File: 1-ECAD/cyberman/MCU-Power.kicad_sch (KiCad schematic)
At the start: 12 parts, among them U1 ESP32-S3R16V

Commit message: update power sche
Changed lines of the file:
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@@
+		)
+	)
+	(text_box "DESIGN NOTE:\nVoltage of VDD_SPI is 1.8V"
+		(exclude_from_sim no)
+		(at 63.5 92.71 0)
+		(size 30.48 20.32)
+		(stroke
+			(width 1)
+			(type solid)
+			(color 200 200 200 1)
+		)
+		(fill
+			(type none)
+		)
+		(effects
+			(font
+				(face "Times New Roman")
+				(size 2 2)
+				(color 0 0 0 1)
+			)
+			(justify left top)
 		)
 	)

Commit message: microSD and LCD connector
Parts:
- U1: Manufacturer (none) -> Espressif; Manufacturer PN (none) -> ESP32-S3R16V; Supplier 1 (none) -> Mouser; Supplier PN 1 (none) -> 356-ESP32-S3R16V; kode PN (none) -> DOTU001
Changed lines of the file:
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@@
 			)
 		)
-		(property "Description" "Xtensa 32-bit dual-core, Wi-Fi/Bluetooth, 16MB PSRAM, 45 GPIOS, QFN56"
+		(property "Description" "Espressif Xtensa 32-bit dual-core, Wi-Fi/Bluetooth, 16MB PSRAM, 45 GPIOS, QFN56"
 			(at 203.2 50.8 0)
 			(effects
@@
 		)
 		(property "kode_PN" "DOTU001"
+			(at 203.2 50.8 0)
+			(effects
+				(font
+					(size 1.27 1.27)
+				)
+				(hide yes)
+			)
+		)
+		(property "kode PN" "DOTU001"
+			(at 203.2 50.8 0)
+			(effects
+				(font
+					(size 1.27 1.27)
+				)
+				(hide yes)
+			)
+		)
+		(property "Manufacturer" "Espressif"
+			(at 203.2 50.8 0)
+			(effects
+				(font
+					(size 1.27 1.27)
+				)
+				(hide yes)
+			)
+		)
+		(property "Manufacturer PN" "ESP32-S3R16V"
+			(at 203.2 50.8 0)
+			(effects
+				(font
+					(size 1.27 1.27)
+				)
+				(hide yes)
+			)
+		)
+		(property "Supplier 1" "Mouser"
+			(at 203.2 50.8 0)
+			(effects
+				(font
+					(size 1.27 1.27)
+				)
+				(hide yes)
+			)
+		)
+		(property "Supplier PN 1" "356-ESP32-S3R16V"
 			(at 203.2 50.8 0)
 			(effects
@@
 			)
 		)
-		(property "Description" "Power symbol creates a global label with name \"VDD_SPI\""
+		(property "Description" "Power symbol creates a global label with name \"VDD\""
 			(at 180.34 73.66 0)
 			(effects

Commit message: esp and usbc footprints
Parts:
- U1: footprint (none) -> 0_mcu_espressif:ESP32-S3R16V
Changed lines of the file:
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@@
 			)
 		)
-		(property "Footprint" ""
+		(property "Footprint" "0_mcu_espressif:ESP32-S3R16V"
 			(at 209.55 38.1 0)
 			(effects

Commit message: footpritn day
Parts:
- U1: Supplier 1 PN (none) -> 356-ESP32-S3R16V; Supplier PN 1 356-ESP32-S3R16V -> (none); kode_PN DOTU001 -> (none)
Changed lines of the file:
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@@
+	)
+	(symbol
+		(lib_id "Device:L")
+		(at 158.75 96.52 90)
+		(unit 1)
+		(exclude_from_sim no)
+		(in_bom yes)
+		(on_board yes)
+		(dnp no)
+		(property "Reference" "L1"
+			(at 154.94 95.25 90)
+			(effects
+				(font
+					(size 1.27 1.27)
+				)
+			)
+		)
+		(property "Value" "2.0nH(0.1nH)"
+			(at 166.37 95.25 90)
+			(effects
+				(font
+					(size 1.27 1.27)
+				)
+			)
+		)
+		(property "Footprint" ""
+			(at 158.75 96.52 0)
+			(effects
+				(font
+					(size 1.27 1.27)
+				)
+				(hide yes)
+			)
+		)
+		(property "Datasheet" "~"
+			(at 158.75 96.52 0)
+			(effects
+				(font
+					(size 1.27 1.27)
+				)
+				(hide yes)
+			)
+		)
+		(property "Description" "Inductor"
+			(at 158.75 96.52 0)
+			(effects
+				(font
+					(size 1.27 1.27)
+				)
+				(hide yes)
+			)
+		)
+		(pin "1"
+		)
+		(pin "2"
+		)
+		(instances
+			(project "cyberman"
+				(path "/0650c7a8-acba-429c-9f8e-eec0baf0bc1c/fede4c36-00cc-4d3d-b71c-5243ba232202/e46a9372-83c8-4117-b39c-2866170a3986"
+					(reference "L1")
+					(unit 1)
+				)
+			)
+		)
 	)
 	(symbol
@@
 			)
 		)
-		(property "kode_PN" "DOTU001"
-			(at 203.2 50.8 0)
-			(effects
-				(font
-					(size 1.27 1.27)
-				)
-				(hide yes)
-			)
-		)
 		(property "kode PN" "DOTU001"
 			(at 203.2 50.8 0)
@@
 			)
 		)
-		(property "Supplier PN 1" "356-ESP32-S3R16V"
+		(property "Supplier 1 PN" "356-ESP32-S3R16V"
 			(at 203.2 50.8 0)
 			(effects
@@
 			)
 		)
+		(pin "2"
+		)
+		(pin "32"
+		)
+		(pin "21"
+		)
+		(pin "47"
+		)
+		(pin "30"
+		)
+		(pin "33"
+		)
+		(pin "34"
+		)
+		(pin "35"
+		)
+		(pin "12"
+		)
+		(pin "25"
+		)
+		(pin "1"
+		)
+		(pin "20"
+		)
+		(pin "53"
+		)
+		(pin "16"
+		)
+		(pin "29"
+		)
+		(pin "3"
+		)
+		(pin "46"
+		)
+		(pin "56"
+		)
+		(pin "57"
+		)
+		(pin "11"
+		)
+		(pin "13"
+		)
+		(pin "14"
+		)
+		(pin "15"
+		)
+		(pin "10"
+		)
+		(pin "17"
+		)
+		(pin "18"
+		)
+		(pin "22"
+		)
+		(pin "24"
+		)
+		(pin "26"
+		)
+		(pin "27"
+		)
+		(pin "23"
+		)
+		(pin "19"
+		)
+		(pin "31"
+		)
+		(pin "6"
+		)
+		(pin "52"
+		)
+		(pin "40"
+		)
+		(pin "43"
+		)
+		(pin "53"
+		)
+		(pin "7"
+		)
+		(pin "49"
+		)
+		(pin "5"
+		)
+		(pin "50"
+		)
+		(pin "44"
+		)
+		(pin "48"
+		)
+		(pin "36"
+		)
+		(pin "51"
+		)
+		(pin "45"
+		)
+		(pin "37"
+		)
+		(pin "42"
+		)
+		(pin "39"
+		)
+		(pin "4"
+		)
+		(pin "38"
+		)
+		(pin "9"
+		)
+		(pin "41"
+		)
+		(pin "8"
+		)
 		(pin "54"
 		)
-		(pin "27"
-		)
-		(pin "10"
-		)
-		(pin "26"
-		)
-		(pin "4"
-		)
-		(pin "53"
-		)
-		(pin "8"
-		)
-		(pin "9"
-		)
-		(pin "47"
-		)
-		(pin "50"
-		)
-		(pin "40"
-		)
-		(pin "44"
-		)
-		(pin "21"
-		)
-		(pin "39"
-		)
-		(pin "41"
-		)
-		(pin "25"
-		)
-		(pin "20"
-		)
-		(pin "31"
-		)
-		(pin "18"
-		)
-		(pin "53"
-		)
-		(pin "33"
-		)
-		(pin "46"
-		)
-		(pin "56"
-		)
-		(pin "19"
-		)
-		(pin "14"
-		)
-		(pin "1"
-		)
-		(pin "13"
-		)
-		(pin "17"
-		)
-		(pin "15"
-		)
-		(pin "48"
-		)
-		(pin "34"
-		)
-		(pin "37"
-		)
-		(pin "42"
-		)
-		(pin "32"
-		)
-		(pin "12"
-		)
-		(pin "57"
-		)
-		(pin "16"
-		)
-		(pin "2"
-		)
-		(pin "36"
-		)
-		(pin "23"
-		)
-		(pin "29"
-		)
-		(pin "22"
-		)
-		(pin "35"
-		)
-		(pin "3"
-		)
-		(pin "38"
-		)
-		(pin "43"
-		)
-		(pin "49"
-		)
-		(pin "5"
-		)
-		(pin "51"
-		)
-		(pin "52"
-		)
-		(pin "45"
-		)
-		(pin "6"
-		)
-		(pin "30"
-		)
-		(pin "24"
-		)
-		(pin "7"
-		)
-		(pin "11"
-		)
-		(instances
-			(project "cyberman"
+		(instances
+			(project ""
 				(path "/0650c7a8-acba-429c-9f8e-eec0baf0bc1c/fede4c36-00cc-4d3d-b71c-5243ba232202/e46a9372-83c8-4117-b39c-2866170a3986"
 					(reference "U1")
-					(unit 1)
-				)
-			)
-		)
-	)
-	(symbol
-		(lib_id "Device:L")
-		(at 158.75 96.52 90)
-		(unit 1)
-		(exclude_from_sim no)
-		(in_bom yes)
-		(on_board yes)
-		(dnp no)
-		(property "Reference" "L1"
-			(at 154.94 95.25 90)
-			(effects
-				(font
-					(size 1.27 1.27)
-				)
-			)
-		)
-		(property "Value" "2.0nH(0.1nH)"
-			(at 166.37 95.25 90)
-			(effects
-				(font
-					(size 1.27 1.27)
-				)
-			)
-		)
-		(property "Footprint" ""
-			(at 158.75 96.52 0)
-			(effects
-				(font
-					(size 1.27 1.27)
-				)
-				(hide yes)
-			)
-		)
-		(property "Datasheet" "~"
-			(at 158.75 96.52 0)
-			(effects
-				(font
-					(size 1.27 1.27)
-				)
-				(hide yes)
-			)
-		)
-		(property "Description" "Inductor"
-			(at 158.75 96.52 0)
-			(effects
-				(font
-					(size 1.27 1.27)
-				)
-				(hide yes)
-			)
-		)
-		(pin "1"
-		)
-		(pin "2"
-		)
-		(instances
-			(project "cyberman"
-				(path "/0650c7a8-acba-429c-9f8e-eec0baf0bc1c/fede4c36-00cc-4d3d-b71c-5243ba232202/e46a9372-83c8-4117-b39c-2866170a3986"
-					(reference "L1")
 					(unit 1)
 				)
@@
 		(dnp no)
 		(fields_autoplaced yes)
-		(property "Reference" "#PWR1"
+		(property "Reference" "#PWR01"
 			(at 215.9 149.86 0)
 			(effects
@@
 			(project "cyberman"
 				(path "/0650c7a8-acba-429c-9f8e-eec0baf0bc1c/fede4c36-00cc-4d3d-b71c-5243ba232202/e46a9372-83c8-4117-b39c-2866170a3986"
-					(reference "#PWR1")
-					(unit 1)
-				)
+					(reference "#PWR01")
+					(unit 1)
+				)

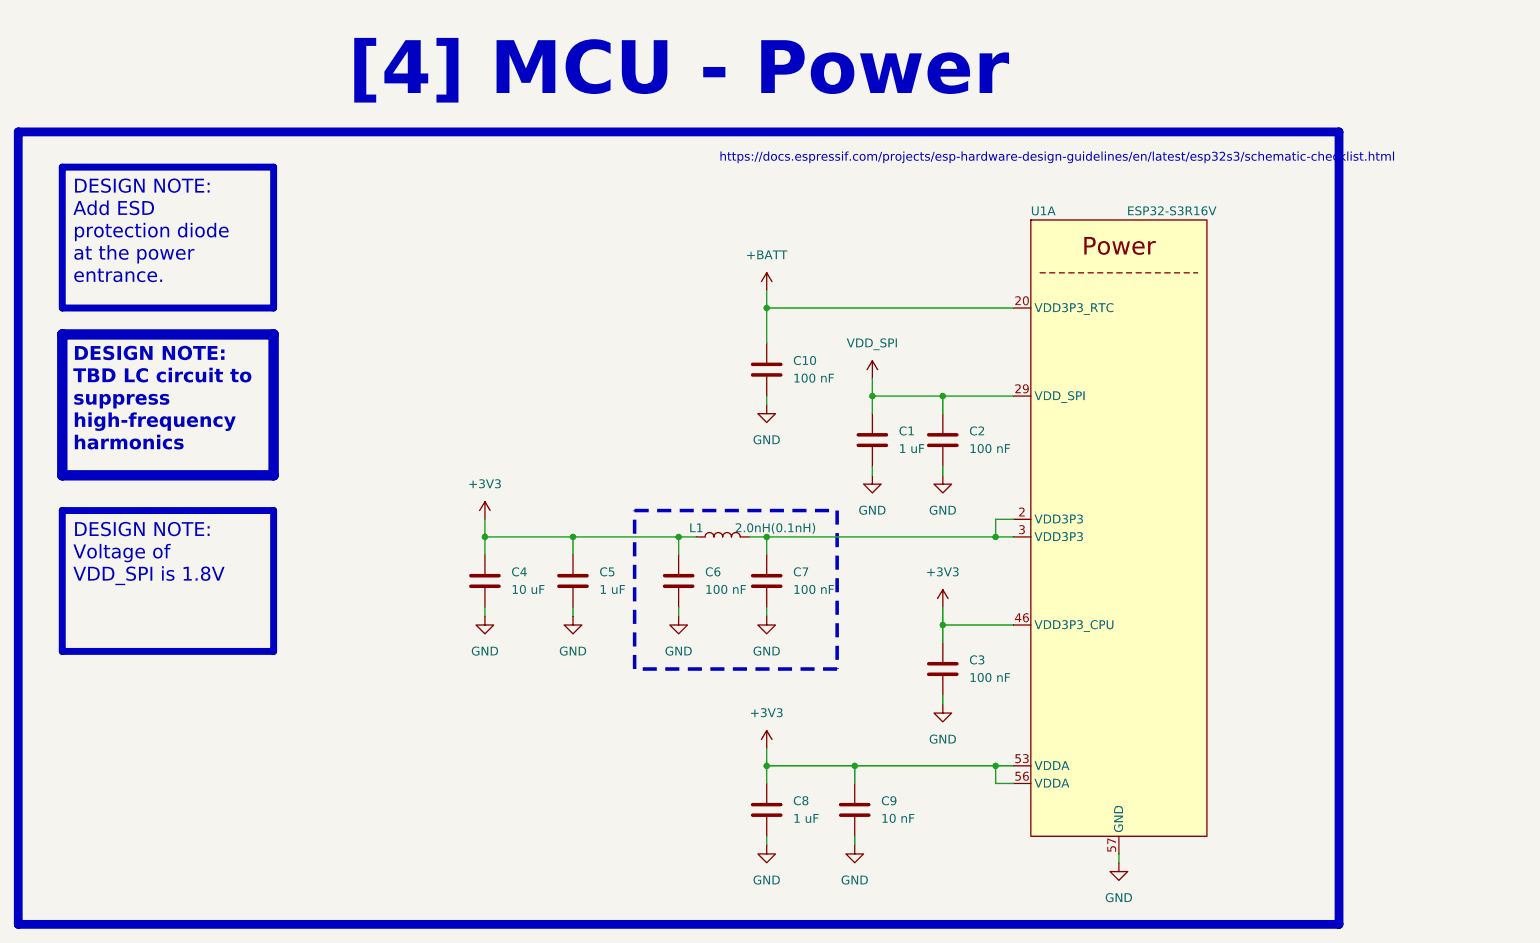
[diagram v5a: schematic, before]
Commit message: new changes
close display page and peripheral schematic
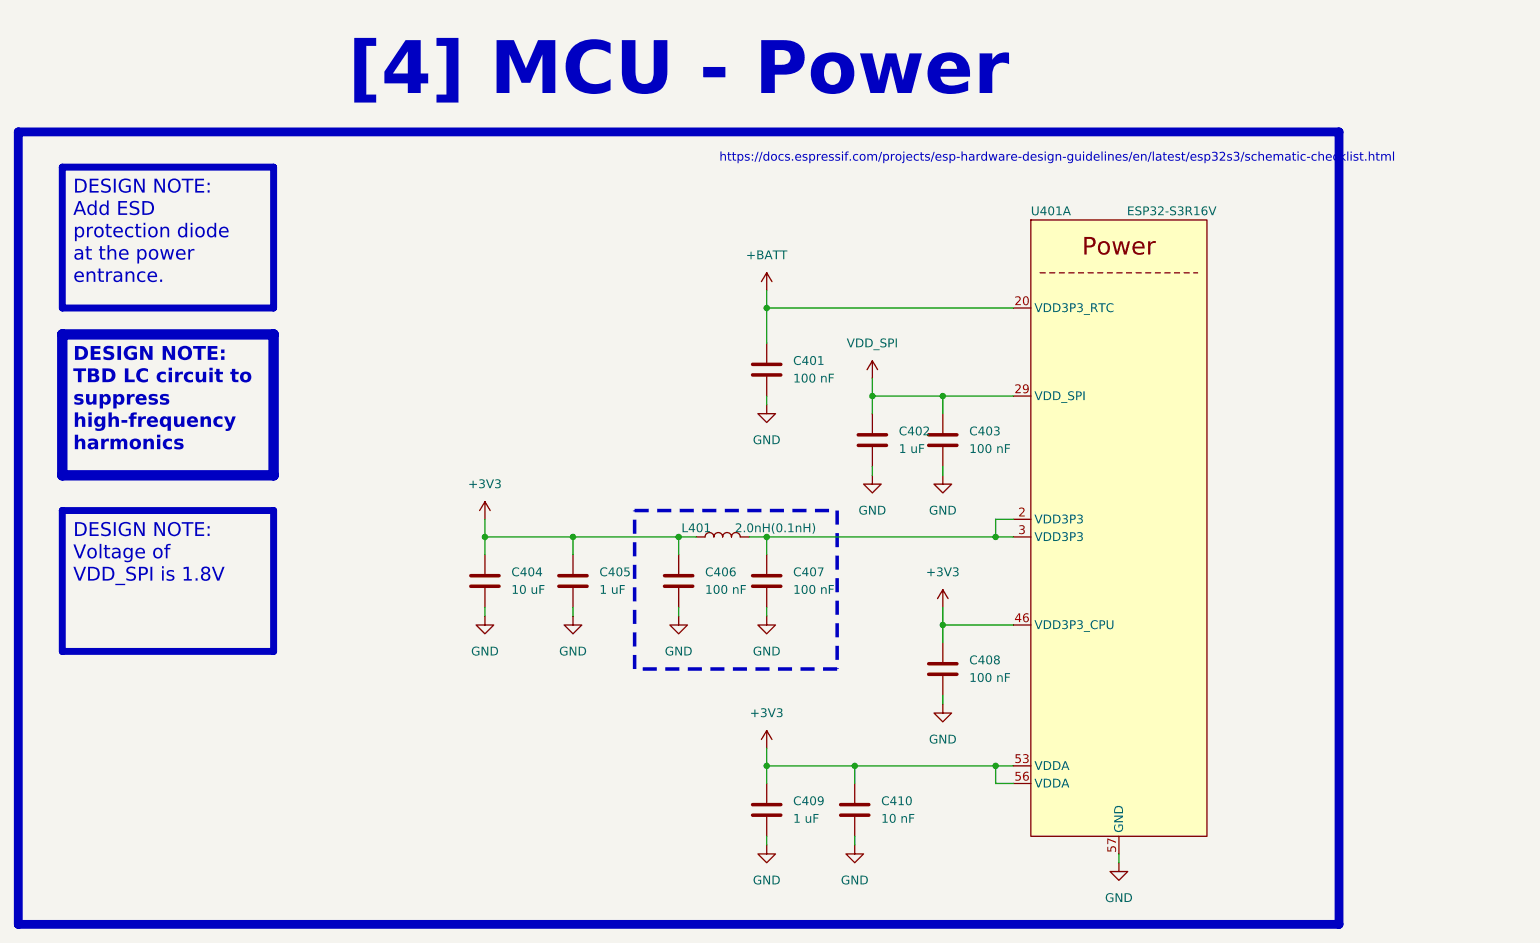
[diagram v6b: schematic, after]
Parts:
- renumbered C10 to C401, C1 to C402, C2 to C403, C4 to C404, C5 to C405, C6 to C406, C7 to C407, C3 to C408, C8 to C409, C9 to C410, L1 to L401, U1 to U401
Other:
- company: (none) -> kode.

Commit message: power page close
siuuuuuuuuuuuu
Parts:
- C401, C403, C406, C407, C408: value 100 nF -> C
- C402, C405, C409: value 1 uF -> C
- C404: value 10 uF -> C
- C410: value 10 nF -> C
- L401: value 2.0nH(0.1nH) -> L
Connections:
- net +BATT renamed +BAT
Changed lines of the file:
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@@
 	(paper "A4")
 	(title_block
-		(date "2024-12-11")
+		(date "2024-12-18")
 		(rev "1.0")
 		(company "kode.")
@@
 			)
 		)
-		(property "Value" "100 nF"
+		(property "Value" "C"
 			(at 168.91 104.14 0)
 			(effects
@@
 		(dnp no)
 		(fields_autoplaced yes)
-		(property "Reference" "#PWR0408"
+		(property "Reference" "#PWR408"
 			(at 124.46 114.3 0)
 			(effects
@@
 			(project "cyberman"
 				(path "/0650c7a8-acba-429c-9f8e-eec0baf0bc1c/fede4c36-00cc-4d3d-b71c-5243ba232202/e46a9372-83c8-4117-b39c-2866170a3986"
-					(reference "#PWR0408")
+					(reference "#PWR408")
 					(unit 1)
 				)
@@
 			)
 		)
-		(property "Value" "100 nF"
+		(property "Value" "C"
 			(at 168.91 73.66 0)
 			(effects
@@
 		(dnp no)
 		(fields_autoplaced yes)
-		(property "Reference" "#PWR0407"
+		(property "Reference" "#PWR407"
 			(at 190.5 110.49 0)
 			(effects
@@
 			(project "cyberman"
 				(path "/0650c7a8-acba-429c-9f8e-eec0baf0bc1c/fede4c36-00cc-4d3d-b71c-5243ba232202/e46a9372-83c8-4117-b39c-2866170a3986"
-					(reference "#PWR0407")
+					(reference "#PWR407")
 					(unit 1)
 				)
@@
 			)
 		)
-		(property "Value" "100 nF"
+		(property "Value" "C"
 			(at 194.31 116.84 0)
 			(effects
@@
 			)
 		)
-		(property "Value" "1 uF"
+		(property "Value" "C"
 			(at 184.15 83.82 0)
 			(effects
@@
 		(dnp no)
 		(fields_autoplaced yes)
-		(property "Reference" "#PWR0401"
+		(property "Reference" "#PWR401"
 			(at 165.1 64.77 0)
 			(effects
@@
 			)
 		)
-		(property "Value" "+BATT"
+		(property "Value" "+BAT"
 			(at 165.1 55.88 0)
 			(effects
@@
 			(project "cyberman"
 				(path "/0650c7a8-acba-429c-9f8e-eec0baf0bc1c/fede4c36-00cc-4d3d-b71c-5243ba232202/e46a9372-83c8-4117-b39c-2866170a3986"
-					(reference "#PWR0401")
+					(reference "#PWR401")
 					(unit 1)
 				)
@@
 			)
 		)
-		(property "Value" "10 uF"
+		(property "Value" "C"
 			(at 128.27 104.14 0)
 			(effects
@@
 		(dnp no)
 		(fields_autoplaced yes)
-		(property "Reference" "#PWR0409"
+		(property "Reference" "#PWR409"
 			(at 137.16 114.3 0)
 			(effects
@@
 			(project "cyberman"
 				(path "/0650c7a8-acba-429c-9f8e-eec0baf0bc1c/fede4c36-00cc-4d3d-b71c-5243ba232202/e46a9372-83c8-4117-b39c-2866170a3986"
-					(reference "#PWR0409")
+					(reference "#PWR409")
 					(unit 1)
 				)
@@
 			)
 		)
-		(property "Value" "1 uF"
+		(property "Value" "C"
 			(at 168.91 137.16 0)
 			(effects
@@
 		(dnp no)
 		(fields_autoplaced yes)
-		(property "Reference" "#PWR0413"
+		(property "Reference" "#PWR413"
 			(at 165.1 130.81 0)
 			(effects
@@
 			(project "cyberman"
 				(path "/0650c7a8-acba-429c-9f8e-eec0baf0bc1c/fede4c36-00cc-4d3d-b71c-5243ba232202/e46a9372-83c8-4117-b39c-2866170a3986"
-					(reference "#PWR0413")
+					(reference "#PWR413")
 					(unit 1)
 				)
@@
 		(dnp no)
 		(fields_autoplaced yes)
-		(property "Reference" "#PWR0411"
+		(property "Reference" "#PWR411"
 			(at 165.1 114.3 0)
 			(effects
@@
 			(project "cyberman"
 				(path "/0650c7a8-acba-429c-9f8e-eec0baf0bc1c/fede4c36-00cc-4d3d-b71c-5243ba232202/e46a9372-83c8-4117-b39c-2866170a3986"
-					(reference "#PWR0411")
+					(reference "#PWR411")
 					(unit 1)
 				)
@@
 		(dnp no)
 		(fields_autoplaced yes)
-		(property "Reference" "#PWR0403"
+		(property "Reference" "#PWR403"
 			(at 165.1 83.82 0)
 			(effects
@@
 			(project "cyberman"
 				(path "/0650c7a8-acba-429c-9f8e-eec0baf0bc1c/fede4c36-00cc-4d3d-b71c-5243ba232202/e46a9372-83c8-4117-b39c-2866170a3986"
-					(reference "#PWR0403")
+					(reference "#PWR403")
 					(unit 1)
 				)
@@
 			)
 		)
-		(property "Value" "100 nF"
+		(property "Value" "C"
 			(at 194.31 83.82 0)
 			(effects
@@
 			)
 		)
-		(property "Value" "2.0nH(0.1nH)"
+		(property "Value" "L"
 			(at 166.37 95.25 90)
 			(effects
@@
 		(dnp no)
 		(fields_autoplaced yes)
-		(property "Reference" "#PWR0404"
+		(property "Reference" "#PWR404"
 			(at 180.34 93.98 0)
 			(effects
@@
 			(project "cyberman"
 				(path "/0650c7a8-acba-429c-9f8e-eec0baf0bc1c/fede4c36-00cc-4d3d-b71c-5243ba232202/e46a9372-83c8-4117-b39c-2866170a3986"
-					(reference "#PWR0404")
+					(reference "#PWR404")
 					(unit 1)
 				)
@@
 		(dnp no)
 		(fields_autoplaced yes)
-		(property "Reference" "#PWR0402"
+		(property "Reference" "#PWR402"
 			(at 180.34 77.47 0)
 			(effects
@@
 			(project "cyberman"
 				(path "/0650c7a8-acba-429c-9f8e-eec0baf0bc1c/fede4c36-00cc-4d3d-b71c-5243ba232202/e46a9372-83c8-4117-b39c-2866170a3986"
-					(reference "#PWR0402")
+					(reference "#PWR402")
 					(unit 1)
 				)
@@
 			)
 		)
-		(property "Value" "100 nF"
+		(property "Value" "C"
 			(at 156.21 104.14 0)
 			(effects
@@
 		(dnp no)
 		(fields_autoplaced yes)
-		(property "Reference" "#PWR0405"
+		(property "Reference" "#PWR405"
 			(at 190.5 93.98 0)
 			(effects
@@
 			(project "cyberman"
 				(path "/0650c7a8-acba-429c-9f8e-eec0baf0bc1c/fede4c36-00cc-4d3d-b71c-5243ba232202/e46a9372-83c8-4117-b39c-2866170a3986"
-					(reference "#PWR0405")
+					(reference "#PWR405")
 					(unit 1)
 				)
@@
 		(dnp no)
 		(fields_autoplaced yes)
-		(property "Reference" "#PWR0412"
+		(property "Reference" "#PWR412"
 			(at 190.5 127 0)
 			(effects
@@
 			(project "cyberman"
 				(path "/0650c7a8-acba-429c-9f8e-eec0baf0bc1c/fede4c36-00cc-4d3d-b71c-5243ba232202/e46a9372-83c8-4117-b39c-2866170a3986"
-					(reference "#PWR0412")
+					(reference "#PWR412")
 					(unit 1)
 				)
@@
 		(dnp no)
 		(fields_autoplaced yes)
-		(property "Reference" "#PWR0416"
+		(property "Reference" "#PWR416"
 			(at 215.9 149.86 0)
 			(effects
@@
 			(project "cyberman"
 				(path "/0650c7a8-acba-429c-9f8e-eec0baf0bc1c/fede4c36-00cc-4d3d-b71c-5243ba232202/e46a9372-83c8-4117-b39c-2866170a3986"
-					(reference "#PWR0416")
+					(reference "#PWR416")
 					(unit 1)
 				)
@@
 		(dnp no)
 		(fields_autoplaced yes)
-		(property "Reference" "#PWR0415"
+		(property "Reference" "#PWR415"
 			(at 177.8 147.32 0)
 			(effects
@@
 			(project "cyberman"
 				(path "/0650c7a8-acba-429c-9f8e-eec0baf0bc1c/fede4c36-00cc-4d3d-b71c-5243ba232202/e46a9372-83c8-4117-b39c-2866170a3986"
-					(reference "#PWR0415")
+					(reference "#PWR415")
 					(unit 1)
 				)
@@
 		(dnp no)
 		(fields_autoplaced yes)
-		(property "Reference" "#PWR0410"
+		(property "Reference" "#PWR410"
 			(at 152.4 114.3 0)
 			(effects
@@
 			(project "cyberman"
 				(path "/0650c7a8-acba-429c-9f8e-eec0baf0bc1c/fede4c36-00cc-4d3d-b71c-5243ba232202/e46a9372-83c8-4117-b39c-2866170a3986"
-					(reference "#PWR0410")
+					(reference "#PWR410")
 					(unit 1)
 				)
@@
 			)
 		)
-		(property "Value" "10 nF"
+		(property "Value" "C"
 			(at 181.61 137.16 0)
 			(effects
@@
 		(dnp no)
 		(fields_autoplaced yes)
-		(property "Reference" "#PWR0414"
+		(property "Reference" "#PWR414"
 			(at 165.1 147.32 0)
 			(effects
@@
 			(project "cyberman"
 				(path "/0650c7a8-acba-429c-9f8e-eec0baf0bc1c/fede4c36-00cc-4d3d-b71c-5243ba232202/e46a9372-83c8-4117-b39c-2866170a3986"
-					(reference "#PWR0414")
+					(reference "#PWR414")
 					(unit 1)
 				)
@@
 			)
 		)
-		(property "Value" "1 uF"
+		(property "Value" "C"
 			(at 140.97 104.14 0)
 			(effects
@@
 		(dnp no)
 		(fields_autoplaced yes)
-		(property "Reference" "#PWR0406"
+		(property "Reference" "#PWR406"
 			(at 124.46 97.79 0)
 			(effects
@@
 			(project "cyberman"
 				(path "/0650c7a8-acba-429c-9f8e-eec0baf0bc1c/fede4c36-00cc-4d3d-b71c-5243ba232202/e46a9372-83c8-4117-b39c-2866170a3986"
-					(reference "#PWR0406")
-					(unit 1)
-				)
+					(reference "#PWR406")
+					(unit 1)
+				)
